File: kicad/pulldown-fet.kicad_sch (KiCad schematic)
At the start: 2 parts, among them Q2 Q_NMOS_GSD

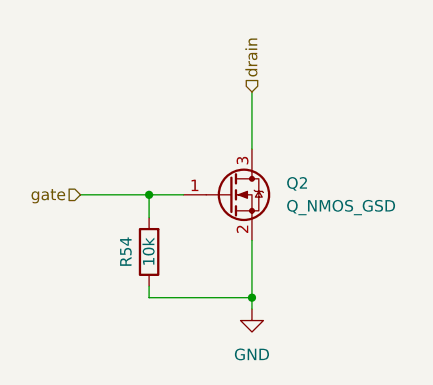
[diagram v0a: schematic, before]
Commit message: added title to all circuit diagrams and sub-circuit diagrams, and PDF export
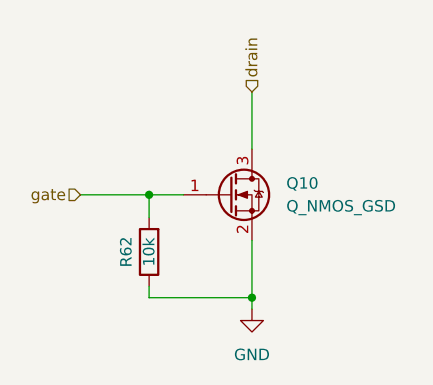
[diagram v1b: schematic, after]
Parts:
- renumbered Q2 to Q10, R54 to R62
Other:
- title: (none) -> pulldown circuit
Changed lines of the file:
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@@
 (kicad_sch (version 20211123) (generator eeschema)
   (paper "A4")
+  (title_block
+    (title "pulldown circuit")
+  )
   (junction (at 120.65 83.82) (diameter 0) (color 0 0 0 0)
   )
@@
   (symbol (lib_id "Device:R") (at 120.65 90.17 180) (unit 1)
     (in_bom yes) (on_board yes)
-    (property "Reference" "R54" (id 0) (at 118.11 90.17 90))
+    (property "Reference" "R62" (id 0) (at 118.11 90.17 90))
     (property "Value" "10k" (id 1) (at 120.65 90.17 90))
     (property "Footprint" "Resistor_SMD:R_0402_1005Metric" (id 2) (at 122.428 90.17 90)
@@
   (symbol (lib_id "Device:Q_NMOS_GSD") (at 129.54 83.82 0) (unit 1)
     (in_bom yes) (on_board yes) (fields_autoplaced)
-    (property "Reference" "Q2" (id 0) (at 135.89 82.5499 0)
+    (property "Reference" "Q10" (id 0) (at 135.89 82.5499 0)
       (effects (font (size 1.27 1.27)) (justify left))
     )
@@
   (symbol (lib_id "power:GND") (at 132.08 96.52 0) (unit 1)
     (in_bom yes) (on_board yes) (fields_autoplaced)
-    (property "Reference" "#PWR094" (id 0) (at 132.08 102.87 0)
+    (property "Reference" "#PWR0102" (id 0) (at 132.08 102.87 0)
       (effects (font (size 1.27 1.27)) hide)
     )

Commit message: new flash, and IEC interface added
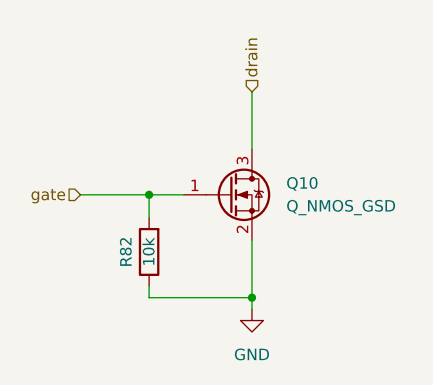
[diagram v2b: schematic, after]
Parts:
- Q10: footprint Package_TO_SOT_SMD:SOT-23 -> Package_DFN_QFN:Diodes_DFN1006-3
- R82: renamed from R62; footprint Resistor_SMD:R_0402_1005Metric -> Resistor_SMD:R_0805_2012Metric
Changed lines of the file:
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@@
   (symbol (lib_id "Device:R") (at 120.65 90.17 180) (unit 1)
     (in_bom yes) (on_board yes)
-    (property "Reference" "R62" (id 0) (at 118.11 90.17 90))
+    (property "Reference" "R82" (id 0) (at 118.11 90.17 90))
     (property "Value" "10k" (id 1) (at 120.65 90.17 90))
-    (property "Footprint" "Resistor_SMD:R_0402_1005Metric" (id 2) (at 122.428 90.17 90)
+    (property "Footprint" "Resistor_SMD:R_0805_2012Metric" (id 2) (at 122.428 90.17 90)
       (effects (font (size 1.27 1.27)) hide)
     )
@@
       (effects (font (size 1.27 1.27)) (justify left))
     )
-    (property "Footprint" "Package_TO_SOT_SMD:SOT-23" (id 2) (at 134.62 81.28 0)
+    (property "Footprint" "Package_DFN_QFN:Diodes_DFN1006-3" (id 2) (at 134.62 81.28 0)
       (effects (font (size 1.27 1.27)) hide)
     )
@@
   (symbol (lib_id "power:GND") (at 132.08 96.52 0) (unit 1)
     (in_bom yes) (on_board yes) (fields_autoplaced)
-    (property "Reference" "#PWR0102" (id 0) (at 132.08 102.87 0)
+    (property "Reference" "#PWR0108" (id 0) (at 132.08 102.87 0)
       (effects (font (size 1.27 1.27)) hide)
     )

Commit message: circuit improvements fixed the level shifter circuit, added the shield pins to the reset button, and replaced the IEC circuit with unused pins of the 16 bit level shifter, and a new 6 channel open collector driver
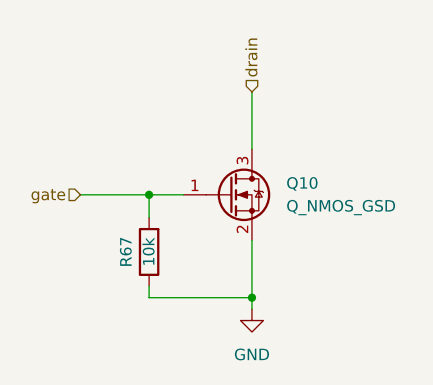
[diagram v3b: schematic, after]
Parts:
- renumbered R82 to R67
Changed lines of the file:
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@@
   (symbol (lib_id "Device:R") (at 120.65 90.17 180) (unit 1)
     (in_bom yes) (on_board yes)
-    (property "Reference" "R82" (id 0) (at 118.11 90.17 90))
+    (property "Reference" "R67" (id 0) (at 118.11 90.17 90))
     (property "Value" "10k" (id 1) (at 120.65 90.17 90))
     (property "Footprint" "Resistor_SMD:R_0805_2012Metric" (id 2) (at 122.428 90.17 90)
@@
   (symbol (lib_id "power:GND") (at 132.08 96.52 0) (unit 1)
     (in_bom yes) (on_board yes) (fields_autoplaced)
-    (property "Reference" "#PWR0108" (id 0) (at 132.08 102.87 0)
+    (property "Reference" "#PWR0112" (id 0) (at 132.08 102.87 0)
       (effects (font (size 1.27 1.27)) hide)
     )
